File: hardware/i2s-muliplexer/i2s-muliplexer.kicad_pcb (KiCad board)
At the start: 2 copper layers, 64.5 x 63.5 mm, 35 parts, among them J1 Conn_01x05, J2 Conn_01x05, J3 Conn_01x05, J4 Conn_01x05, J5 Conn_01x05, J6 Conn_01x05, J7 Conn_01x07, J8 Conn_01x05, U1 74HC244, U2 74HC244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

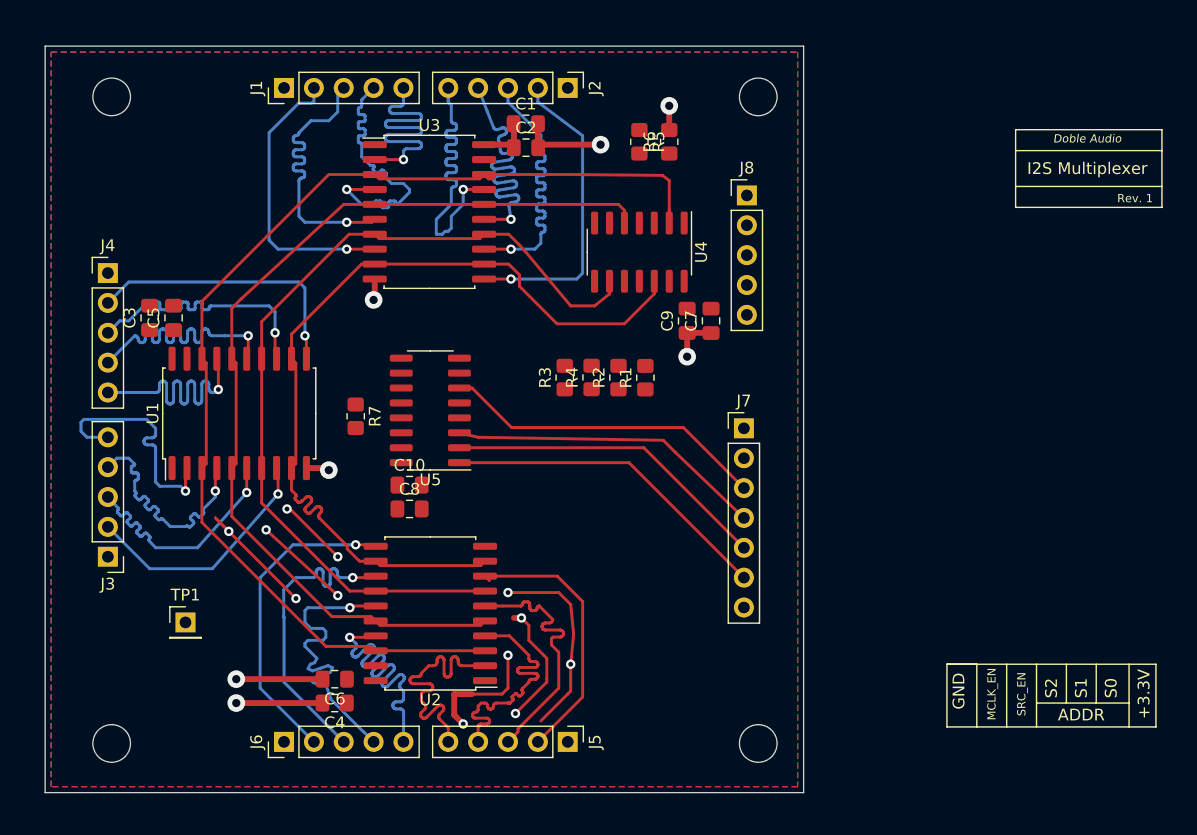
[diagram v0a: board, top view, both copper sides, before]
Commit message: Layout with double row connectors
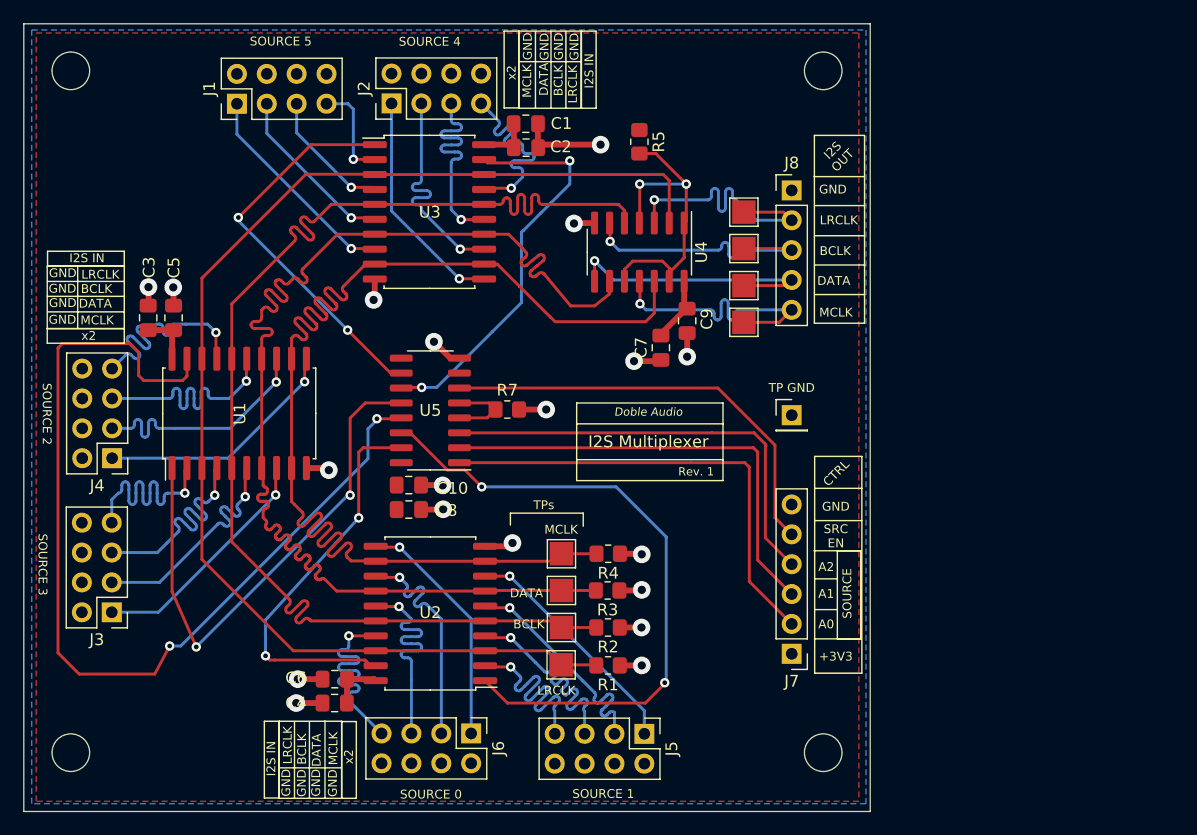
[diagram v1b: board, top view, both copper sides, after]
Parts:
- removed R6: 10K, Resistor_SMD:R_0805_2012Metric_Pad1.20x1.40mm_HandSolder
- removed REF** (x4): MountingHole_3.2mm_M3_ISO7380, MountingHole:MountingHole_3.2mm_M3_ISO7380
- added H1: MountingHole, MountingHole:MountingHole_3.2mm_M3_DIN965, F.Cu at (54.0, 75.0)
- added H2: MountingHole, MountingHole:MountingHole_3.2mm_M3_DIN965, F.Cu at (54.0, 133.0)
- added H3: MountingHole, MountingHole:MountingHole_3.2mm_M3_DIN965, F.Cu at (118.0, 75.0)
- added H4: MountingHole, MountingHole:MountingHole_3.2mm_M3_DIN965, F.Cu at (118.0, 133.0)
- added TP2: TestPoint, TestPoint:TestPoint_Pad_2.0x2.0mm, F.Cu at (95.7, 125.5)
- added TP3: TestPoint, TestPoint:TestPoint_Pad_2.0x2.0mm, F.Cu at (95.7, 122.4)
- added TP4: TestPoint, TestPoint:TestPoint_Pad_2.0x2.0mm, F.Cu at (95.7, 119.2)
- added TP5: TestPoint, TestPoint:TestPoint_Pad_2.0x2.0mm, F.Cu at (95.7, 116.1)
- added TP6: TestPoint, TestPoint:TestPoint_Pad_2.0x2.0mm, F.Cu at (111.3, 87.0)
- added TP7: TestPoint, TestPoint:TestPoint_Pad_2.0x2.0mm, F.Cu at (111.3, 90.1)
- added TP8: TestPoint, TestPoint:TestPoint_Pad_2.0x2.0mm, F.Cu at (111.3, 93.3)
- added TP9: TestPoint, TestPoint:TestPoint_Pad_2.0x2.0mm, F.Cu at (111.3, 96.4)
- J1, J2, J3, J4, J5, J6: value Conn_01x05 -> Conn_02x04_Odd_Even; footprint Connector_PinHeader_2.54mm:PinHeader_1x05_P2.54mm_Vertical -> Connector_PinHeader_2.54mm:PinHeader_2x04_P2.54mm_Vertical
- J7: value Conn_01x07 -> Conn_01x06; footprint Connector_PinHeader_2.54mm:PinHeader_1x07_P2.54mm_Vertical -> Connector_PinHeader_2.54mm:PinHeader_1x06_P2.54mm_Vertical
- TP GND: renamed from TP1
- moved TP GND 54.5 mm to (115.3, 104.3)
- moved R1 24.7 mm to (99.7, 125.6), turned to 180 degrees
- moved R2 21.3 mm to (99.7, 122.4), turned to 180 degrees
- moved J7 19.6 mm to (115.3, 124.6), turned to 180 degrees
- moved R3 18.5 mm to (99.7, 119.2), turned to 180 degrees
- moved J6 15.9 mm to (88.1, 131.4), turned to -90 degrees
- moved J4 15.8 mm to (57.5, 108.0), turned to 180 degrees
- moved R4 15.1 mm to (99.7, 116.1), turned to 180 degrees
- moved J2 15.0 mm to (81.3, 77.8), turned to 90 degrees
- moved R7 12.9 mm to (91.1, 103.8), turned to 0 degrees
- moved J5 6.55 mm to (102.8, 131.4)
- moved C7 4.84 mm to (104.2, 98.6)
- moved J3 4.74 mm to (57.5, 121.1)
- moved J1 4.23 mm to (68.1, 77.8)
- moved J8 3.84 mm to (115.3, 85.2)
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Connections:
- J1 pad 1: GND -> MCLK_5
- J1 pad 2: MCLK_5 -> GND
- J1 pad 4: BCLK_5 -> GND
- J1 pad 5: LRCLK_5 -> BCLK_5
- J2 pad 1: GND -> MCLK_4
- J2 pad 2: MCLK_4 -> GND
- J2 pad 4: BCLK_4 -> GND
- J2 pad 5: LRCLK_4 -> BCLK_4
- J3 pad 1: GND -> MCLK_3
- J3 pad 2: MCLK_3 -> GND
- J3 pad 4: BCLK_3 -> GND
- J3 pad 5: LRCLK_3 -> BCLK_3
- J4 pad 1: GND -> MCLK_2
- J4 pad 2: MCLK_2 -> GND
- J4 pad 4: BCLK_2 -> GND
- J4 pad 5: LRCLK_2 -> BCLK_2
- J5 pad 1: GND -> MCLK_1
- J5 pad 2: MCLK_1 -> GND
- J5 pad 4: BCLK_1 -> GND
- J5 pad 5: LRCLK_1 -> BCLK_1
- J6 pad 1: GND -> MCLK_0
- J6 pad 2: MCLK_0 -> GND
- J6 pad 4: BCLK_0 -> GND
- J6 pad 5: LRCLK_0 -> BCLK_0
- J7 pad 1: GND -> +3V3
- J7 pad 2: MCLK_EN -> A0
- J7 pad 3: SRC_EN -> A1
- J7 pad 5: A1 -> SRC_EN
- J7 pad 6: A0 -> GND
- J8 pad 2: MCLK_OUT -> LRCLK_OUT
- J8 pad 5: LRCLK_OUT -> MCLK_OUT
- U4 pad 13: MCLK_EN -> Net-(R5-Pad2)
- U5 pad 7: Net-(U5-Pad7) -> unconnected-(U5-Pad7)
- U5 pad 9: Net-(U5-Pad9) -> unconnected-(U5-Pad9)
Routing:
- net /CH_EN_2: track 0.00 -> 82.1 mm, vias 0 -> 2
- net /CH_EN_1: track 0.00 -> 55.5 mm, vias 0 -> 2
- net GND: track 95.7 -> 44.2 mm
- net /CH_EN_3: track 0.00 -> 45.5 mm, vias 0 -> 2
- net /CH_EN_4: track 0.00 -> 34.5 mm, vias 0 -> 2
- net /DATA: track 74.7 -> 108.8 mm
- net /CH_EN_0: track 0.00 -> 33.9 mm, vias 0 -> 2
- net /CH_EN_5: track 0.00 -> 33.7 mm, vias 0 -> 2
- net /MCLK: track 74.4 -> 107.8 mm
- net Net-(R5-Pad2): track 0.00 -> 27.7 mm, vias 0 -> 2
- net /BCLK: track 81.7 -> 107.9 mm
- net MCLK_OUT: track 0.00 -> 23.6 mm, vias 0 -> 1
- net LRCLK_OUT: track 0.00 -> 23.5 mm, vias 0 -> 1
- net DATA_OUT: track 0.00 -> 23.4 mm, vias 0 -> 1
- net BCLK_OUT: track 0.00 -> 23.2 mm, vias 0 -> 1
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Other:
- board size 64.5 x 63.5 mm -> 72 x 67 mm
- board text added: "+3V3"
- board text added: "A0"
- board text added: "A1"
- board text added: "A2"
- board text added: "BCLK"
- board text added: "CTRL"
- board text added: "DATA"
- board text added: "I2S IN"
- board text added: "I2S OUT"
- board text added: "LRCLK"
- board text added: "MCLK"
- board text added: "SOURCE"
- board text added: "SOURCE 0"
- board text added: "SOURCE 1"
- board text added: "SOURCE 2"
- board text added: "SOURCE 3"
- board text added: "SOURCE 4"
- board text added: "SOURCE 5"
- board text added: "SRC EN"
- board text added: "TPs"
- board text added: "x2"
- board text removed: "+3.3V"
- board text removed: "ADDR"
- board text removed: "MCLK_EN"
- board text removed: "S0"
- board text removed: "S1"
- board text removed: "S2"
- board text removed: "SRC_EN"

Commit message: Added symbols and adjusted silkscreen
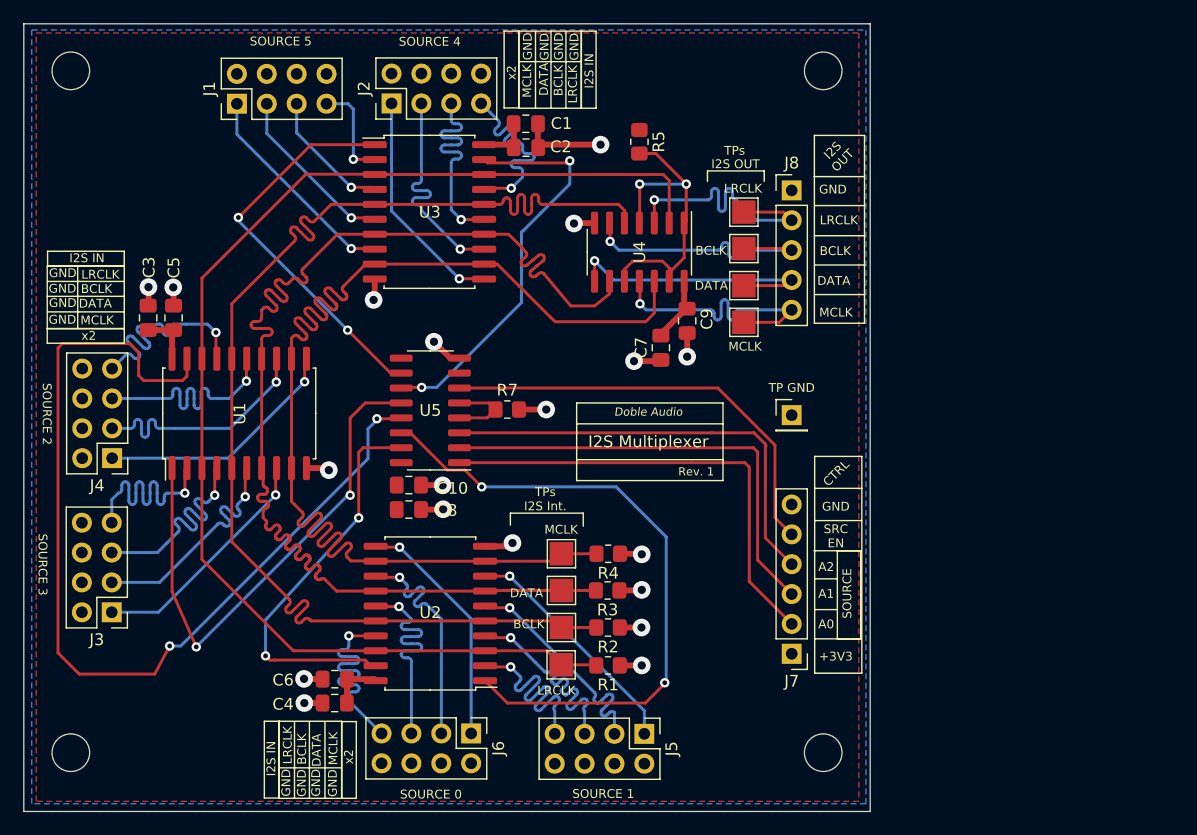
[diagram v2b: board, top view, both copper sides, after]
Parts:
- added REF**: OSHW-Logo2_7.3x6mm_SilkScreen, Symbol:OSHW-Logo2_7.3x6mm_SilkScreen, B.Cu at (60.8, 80.5)
- added REF**: KiCad-Logo2_5mm_SilkScreen, Symbol:KiCad-Logo2_5mm_SilkScreen, B.Cu at (60.1, 86.4)
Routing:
- net GND: track 44.2 -> 43.0 mm
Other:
- board text added: "TPs I2S Int."
